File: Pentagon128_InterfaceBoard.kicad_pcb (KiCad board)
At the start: 2 copper layers, 150 x 119 mm, 40 parts, among them J1 DIN41612_02x32_AB, J10 Tape Out, J11 Tape In, J12 Mini-DIN-6, J14 Barrel_Jack_Switch, J2 Conn_02x03_Odd_Even ATmega Pr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, J3 Conn_02x08_Odd_Even Ext Keyb, J4 Conn_02x05_Odd_Even Kempston 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, J5 DE9_Plug Kempston Out SMD, J6 DE15_Plug_HighDensity VGA CRT, J7 Conn_01x04 FDD Power, J8 Conn_01x04 Audio In, J9 AudioJack3, Q1 Q_NPN_BCE, Q2 Q_NPN_BCE, Q3 Q_NPN_BCE, Q4 Q_NPN_BCE, U1 MT8816 PLCC44, U2 ATmega168PA-A

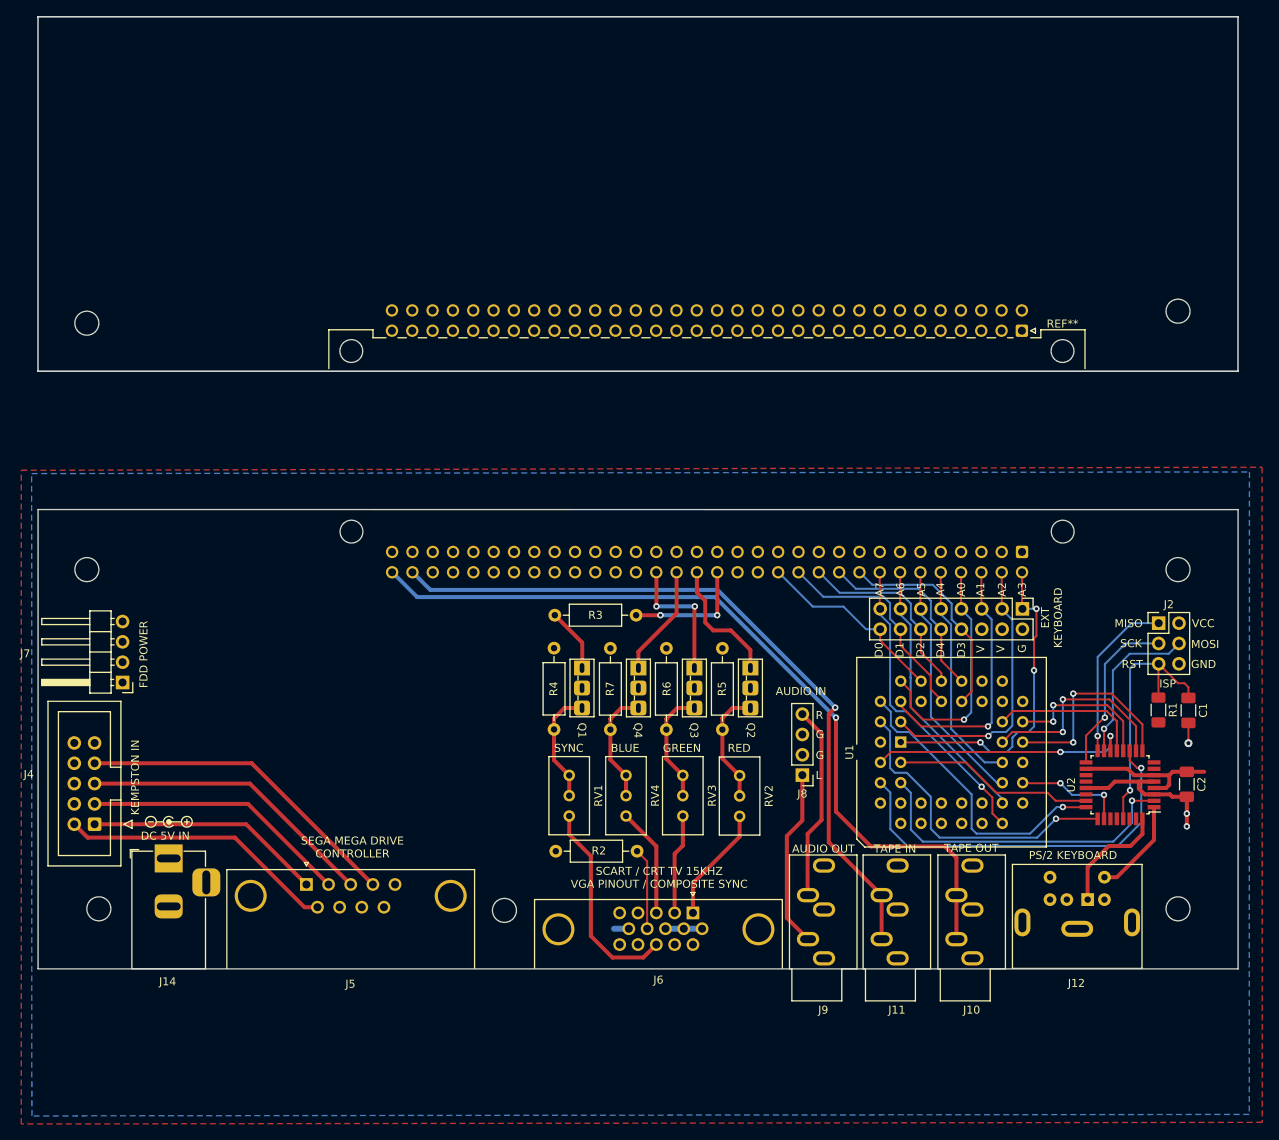
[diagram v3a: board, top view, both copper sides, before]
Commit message: Extend board height from 57.4 mm to 60 mm.
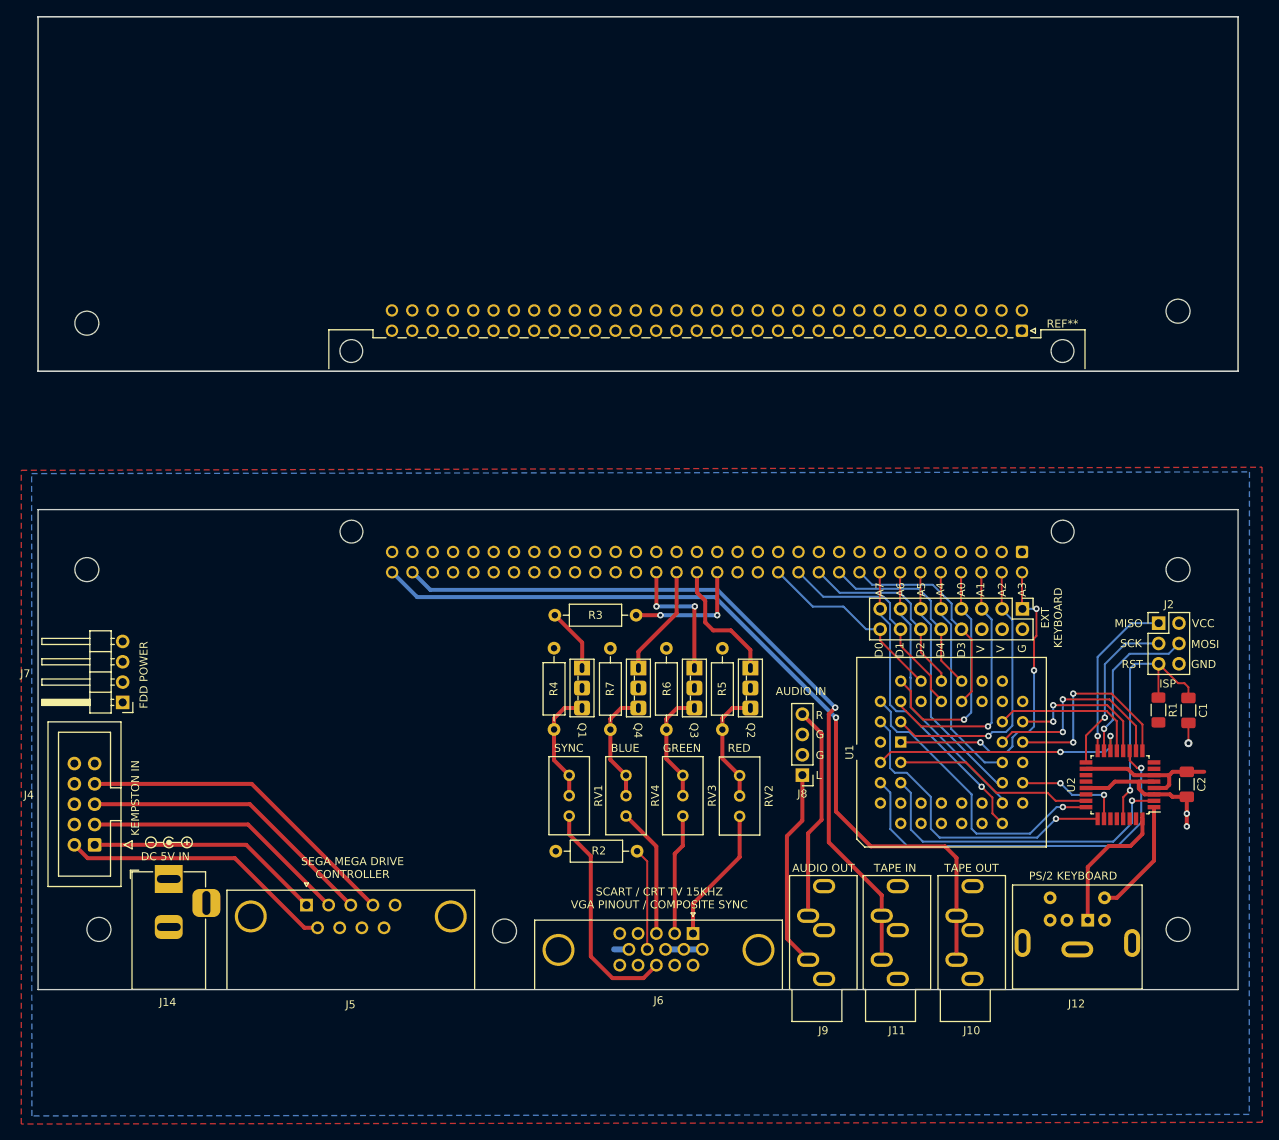
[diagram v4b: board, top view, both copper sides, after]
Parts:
- moved J10 2.58 mm to (171.4, 117.0)
- moved J11 2.58 mm to (162.1, 117.0)
- moved J12 2.58 mm to (185.8, 109.6)
- moved J4 2.58 mm to (61.7, 100.2)
- moved J5 2.58 mm to (88.2, 107.7)
- moved J6 2.58 mm to (136.5, 111.3)
- moved J9 2.58 mm to (152.9, 117.0)
- moved REF** 2.58 mm to (62.2, 110.8)
- moved REF** 2.58 mm to (197.1, 110.8)
- moved J14 2.58 mm to (70.9, 104.5)
- moved REF** 2.58 mm to (112.9, 111.0)
- moved J7 2.49 mm to (65.2, 82.4)
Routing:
- net /CRT_SYNC: track 26.1 -> 28.7 mm
- net /TAPE_OUT: track 102.3 -> 104.9 mm
- net /TAPE_IN: track 91.8 -> 94.4 mm
- net Net-(J6-Pad9): track 10.2 -> 12.8 mm
- net /CRT_RED: track 14.5 -> 17.1 mm
- net /CLK: track 12.2 -> 14.8 mm
- net /DAT: track 14.5 -> 17.1 mm
- net /CRT_GREEN: track 12.5 -> 15.1 mm
- net /AUDIO_LEFT: track 22.4 -> 25.0 mm
- net /CRT_BLUE: track 13.7 -> 16.2 mm
- net /AUDIO_RIGHT: track 24.3 -> 26.9 mm
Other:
- board size 150 x 119 mm -> 150 x 121.6 mm

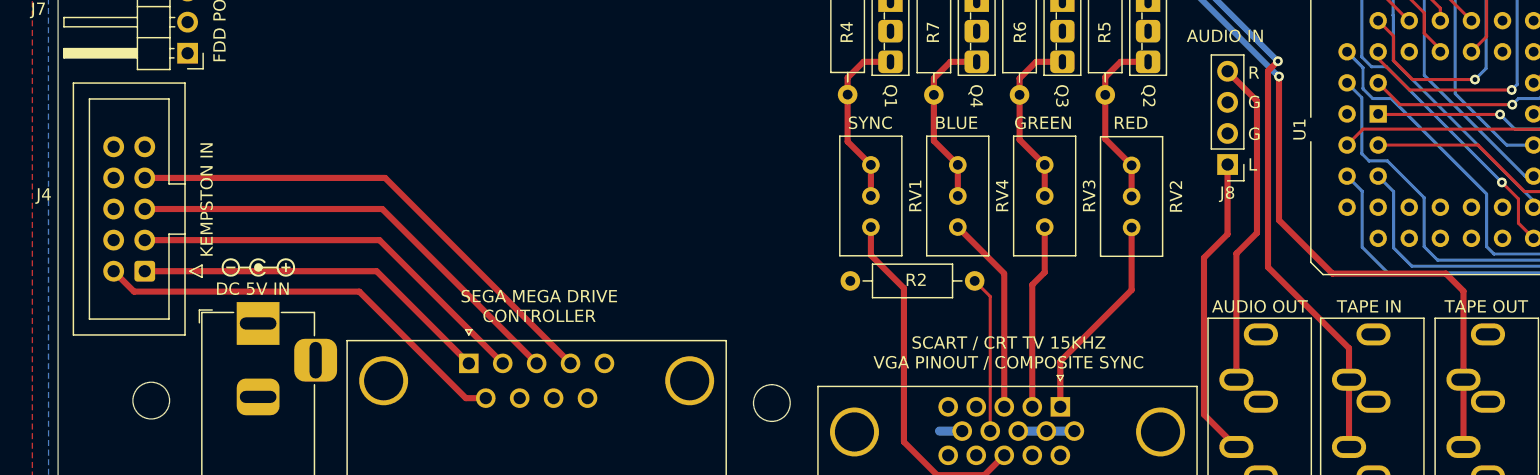
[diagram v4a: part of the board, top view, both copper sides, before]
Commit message: Move KEMPSTON_IN connector closer to Sega Mega Drive Controller connector. Orientation to better fit connecting flat cable.
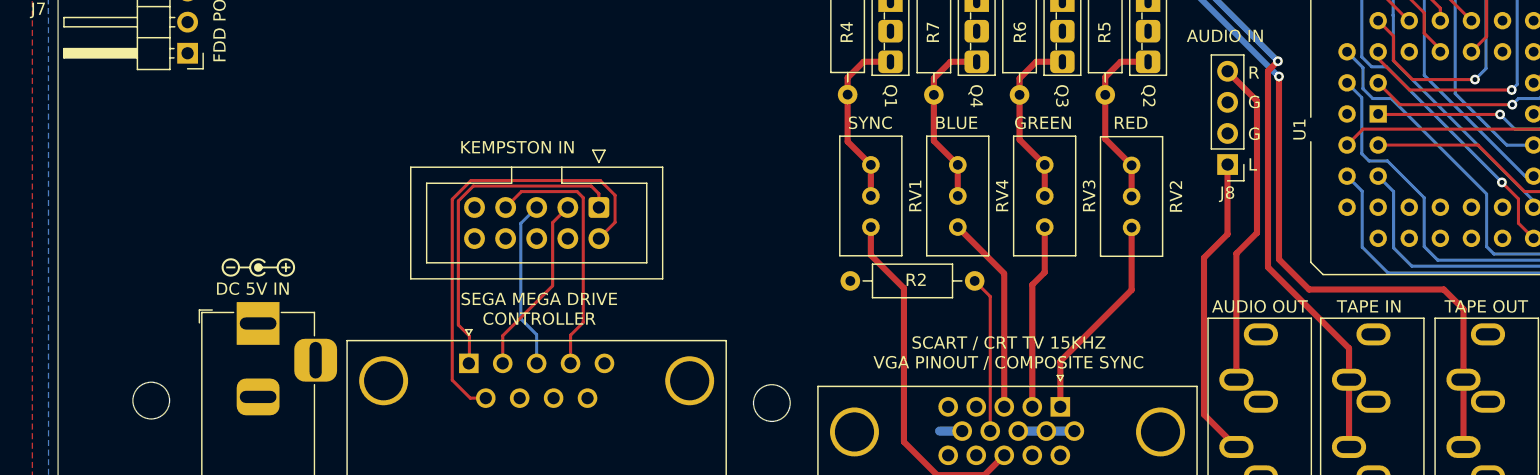
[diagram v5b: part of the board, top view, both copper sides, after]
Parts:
- moved J4 37.5 mm to (98.8, 95.0), turned to -90 degrees
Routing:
- net /LEFT: track 37.2 -> 13.8 mm
- net /RIGHT: track 41.1 -> 21.0 mm
- net /DOWN: track 33.4 -> 14.9 mm
- net /UP: track 29.6 -> 27.0 mm
- net /FIRE: track 34.7 -> 36.6 mm
- net /TAPE_OUT: track 104.9 -> 105.9 mm

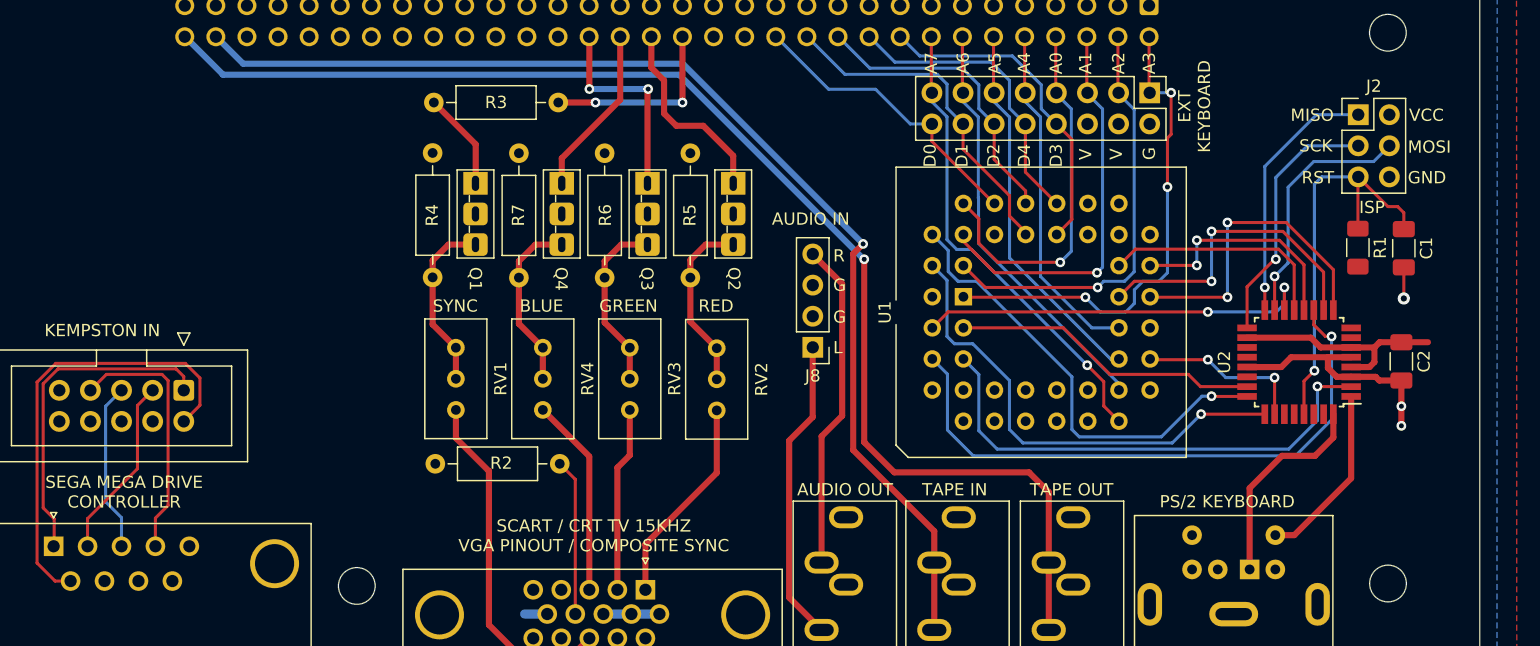
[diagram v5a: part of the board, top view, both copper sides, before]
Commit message: Move PS/2 keyboard controller down. Align EXT_KEYBOARD connector markings. Fix DRC errors. Additional fill exclude zones.
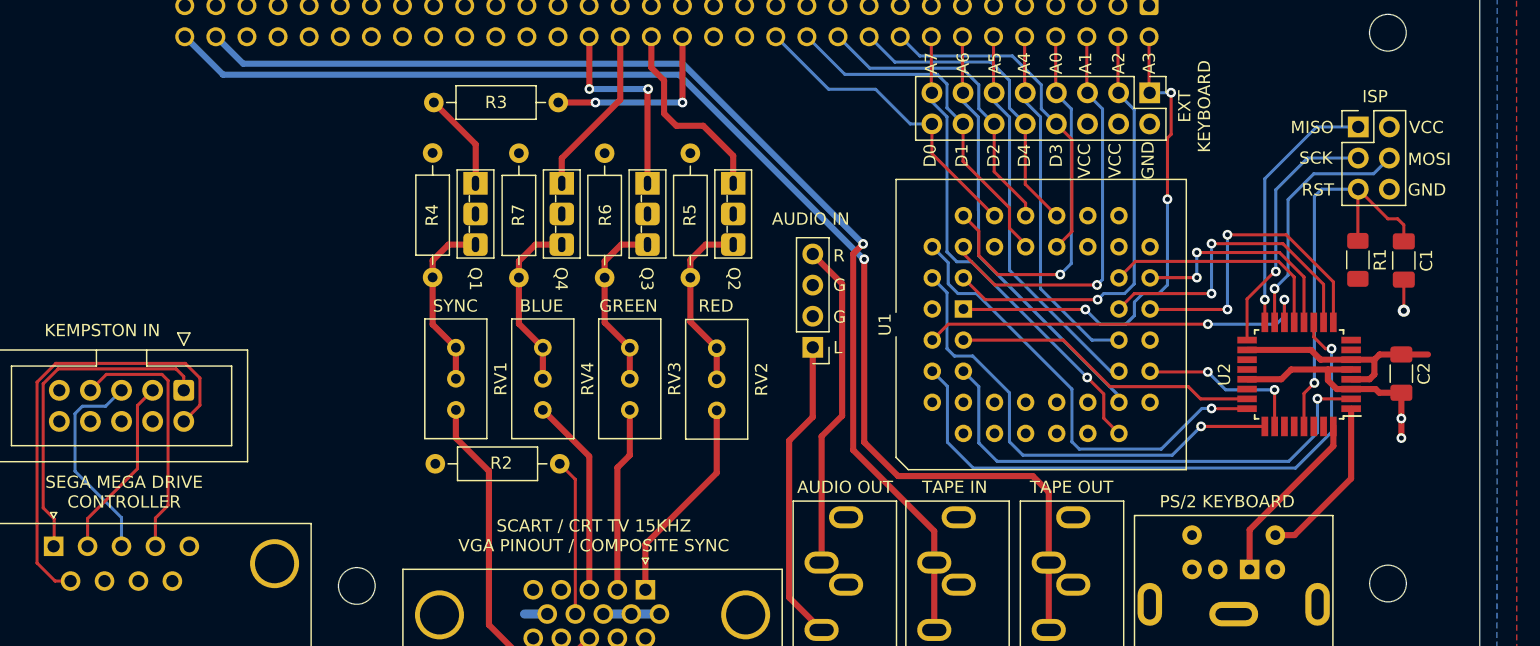
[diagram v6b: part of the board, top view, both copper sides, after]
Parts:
- moved C1 1.00 mm to (198.4, 84.4)
- moved C2 1.00 mm to (198.2, 93.6)
- moved J2 1.00 mm to (194.7, 73.5)
- moved R1 1.00 mm to (194.7, 84.3)
- moved U1 1.00 mm to (162.4, 88.4)
- moved U2 1.00 mm to (189.8, 93.7)
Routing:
- net /LEFT: track 13.8 -> 17.0 mm
- net /DAT: track 17.1 -> 14.5 mm
- net /X4: track 24.4 -> 25.5 mm
- net /Y0: track 30.4 -> 31.4 mm
- net /X1: track 28.0 -> 29.0 mm
- net /Y7: track 38.5 -> 39.5 mm
- net /Y6: track 34.2 -> 35.2 mm
- net /Y5: track 31.1 -> 32.1 mm
- net /Y4: track 28.3 -> 29.3 mm
- net /Y3: track 40.1 -> 41.1 mm
- net /Y2: track 35.0 -> 36.0 mm
- net /Y1: track 32.6 -> 33.6 mm
- net /X3: track 26.9 -> 27.9 mm
- net /X2: track 24.4 -> 25.4 mm
- net /X0: track 24.3 -> 25.3 mm
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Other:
- board text removed: "V"
